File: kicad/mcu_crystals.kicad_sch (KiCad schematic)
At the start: 6 parts, among them X1 32MHz, X2 32kHz768

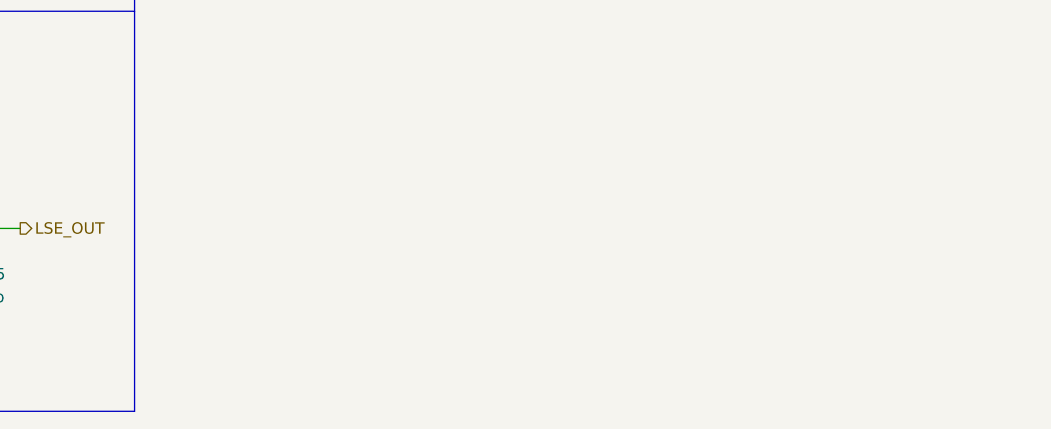
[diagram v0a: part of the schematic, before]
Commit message: feat(BOM): fill missing parts in BOM
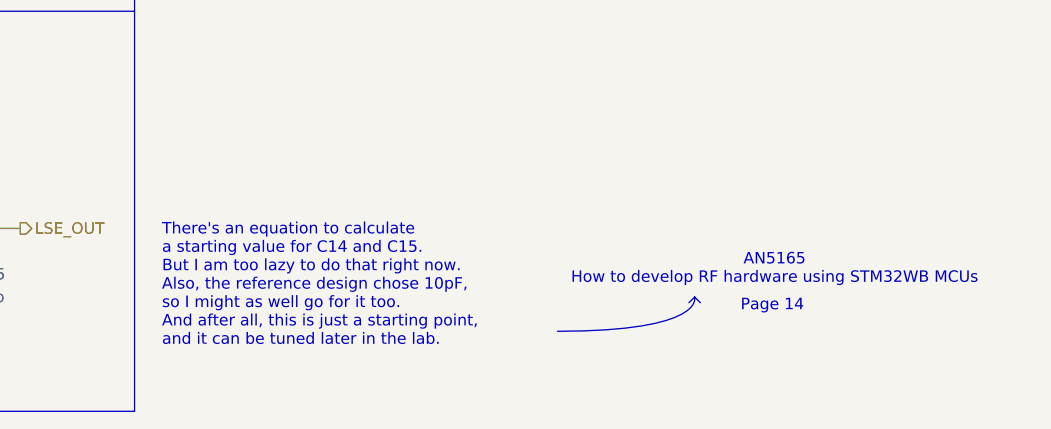
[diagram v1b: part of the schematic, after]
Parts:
- C14, C15: Distributor (none) -> LCSC; Distributor Link (none) -> https://www.lcsc.com/product-detail/C161520.html; MPN (none) -> GRM1555C1H100FA01D; Manufacturer (none) -> muRata
- R1, R2: Distributor (none) -> LCSC; Distributor Link (none) -> https://www.lcsc.com/product-detail/C190119.html; MPN (none) -> CRCW04020000Z0ED; Manufacturer (none) -> VISHAY
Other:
- note added: "AN5165 How to develop RF hardware using STM32WB MCUs"
- note added: "Page 14"
- note added: "There's an equation to calculate a starting value for C14 and C15. But I am too lazy to do that right now. Also, the reference design chose 10pF, so I might as well go for it too. And after all, this is just a starting point, and it can be tuned later in the lab."
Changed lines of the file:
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@@
 		(comment 4 "GitHub: https://github.com/odaij/stm32-bt-board")
+	)
+	(bezier
+		(pts
+			(xy 232.41 137.16) (xy 248.92 137.16) (xy 247.65 133.35) (xy 247.65 133.35)
+		)
+		(stroke
+			(width 0)
+			(type default)
+		)
+		(fill
+			(type none)
+		)
 	)
 	(rectangle
@@
 				(bold yes)
 			)
+		)
+	)
+	(text "Page 14"
+		(exclude_from_sim no)
+		(at 256.286 134.366 0)
+		(effects
+			(font
+				(size 1.27 1.27)
+			)
+		)
+	)
+	(text "AN5165\nHow to develop RF hardware using STM32WB MCUs\n"
+		(exclude_from_sim no)
+		(at 256.54 130.302 0)
+		(effects
+			(font
+				(size 1.27 1.27)
+			)
+			(href "https://www.st.com/resource/en/application_note/an5165-how-to-develop-rf-hardware-using-stm32wb-microcontrollers-stmicroelectronics.pdf")
+		)
+	)
+	(text "There's an equation to calculate\na starting value for C14 and C15.\nBut I am too lazy to do that right now.\nAlso, the reference design chose 10pF,\nso I might as well go for it too.\nAnd after all, this is just a starting point,\nand it can be tuned later in the lab."
+		(exclude_from_sim no)
+		(at 188.468 132.08 0)
+		(effects
+			(font
+				(size 1.27 1.27)
+			)
+			(justify left)
 		)
 	)
@@
 		(pts
 			(xy 163.83 135.89) (xy 163.83 138.43)
+		)
+		(stroke
+			(width 0)
+			(type default)
+		)
+	)
+	(polyline
+		(pts
+			(xy 247.65 133.35) (xy 248.285 133.985)
+		)
+		(stroke
+			(width 0)
+			(type default)
+		)
+	)
+	(polyline
+		(pts
+			(xy 247.015 133.985) (xy 247.65 133.35)
 		)
 		(stroke
@@
 			)
 		)
-		(property "Datasheet" ""
+		(property "Datasheet" "https://www.lcsc.com/datasheet/C190119.pdf"
 			(at 140.97 80.01 0)
 			(hide yes)
@@
 			)
 		)
-		(property "Description" "Resistor, small symbol"
+		(property "Description" "RES 0Ω 62.5mW 0402"
 			(at 140.97 80.01 0)
 			(hide yes)
@@
 			)
 		)
-		(property "Distributor" ""
+		(property "Distributor" "LCSC"
+			(at 140.97 80.01 90)
+			(hide yes)
+			(show_name no)
+			(do_not_autoplace no)
+			(effects
+				(font
+					(size 1.27 1.27)
+				)
+			)
+		)
+		(property "Distributor Link" "https://www.lcsc.com/product-detail/C190119.html"
+			(at 140.97 80.01 90)
+			(hide yes)
+			(show_name no)
+			(do_not_autoplace no)
+			(effects
+				(font
+					(size 1.27 1.27)
+				)
+			)
+		)
+		(property "MPN" "CRCW04020000Z0ED"
+			(at 140.97 80.01 90)
+			(hide yes)
+			(show_name no)
+			(do_not_autoplace no)
+			(effects
+				(font
+					(size 1.27 1.27)
+				)
+			)
+		)
+		(property "Manufacturer" "VISHAY"
 			(at 140.97 80.01 90)
 			(hide yes)
@@
 			)
 		)
-		(property "Datasheet" ""
+		(property "Datasheet" "https://www.lcsc.com/datasheet/C161520.pdf"
 			(at 163.83 132.08 0)
 			(hide yes)
@@
 			)
 		)
-		(property "Description" "Unpolarized capacitor"
+		(property "Description" "CAP CER 10pF 50V C0G 0402"
 			(at 163.83 132.08 0)
 			(hide yes)
@@
 			)
 		)
-		(property "Distributor Link" ""
+		(property "Distributor Link" "https://www.lcsc.com/product-detail/C161520.html"
 			(at 163.83 132.08 0)
 			(hide yes)
@@
 			)
 		)
-		(property "Manufacturer" ""
+		(property "Manufacturer" "muRata"
 			(at 163.83 132.08 0)
 			(hide yes)
@@
 			)
 		)
-		(property "Distributor" ""
+		(property "Distributor" "LCSC"
+			(at 163.83 132.08 0)
+			(hide yes)
+			(show_name no)
+			(do_not_autoplace no)
+			(effects
+				(font
+					(size 1.27 1.27)
+				)
+			)
+		)
+		(property "MPN" "GRM1555C1H100FA01D"
 			(at 163.83 132.08 0)
 			(hide yes)
@@
 			)
 		)
-		(property "Datasheet" ""
+		(property "Datasheet" "https://www.lcsc.com/datasheet/C161520.pdf"
 			(at 147.32 132.08 0)
 			(hide yes)
@@
 			)
 		)
-		(property "Description" "Unpolarized capacitor"
+		(property "Description" "CAP CER 10pF 50V C0G 0402"
 			(at 147.32 132.08 0)
 			(hide yes)
@@
 			)
 		)
-		(property "Distributor Link" ""
+		(property "Distributor Link" "https://www.lcsc.com/product-detail/C161520.html"
 			(at 147.32 132.08 0)
 			(hide yes)
@@
 			)
 		)
-		(property "Manufacturer" ""
+		(property "Manufacturer" "muRata"
 			(at 147.32 132.08 0)
 			(hide yes)
@@
 			)
 		)
-		(property "Distributor" ""
+		(property "Distributor" "LCSC"
+			(at 147.32 132.08 0)
+			(hide yes)
+			(show_name no)
+			(do_not_autoplace no)
+			(effects
+				(font
+					(size 1.27 1.27)
+				)
+			)
+		)
+		(property "MPN" "GRM1555C1H100FA01D"
 			(at 147.32 132.08 0)
 			(hide yes)
@@
 			)
 		)
-		(property "Datasheet" ""
+		(property "Datasheet" "https://www.lcsc.com/datasheet/C190119.pdf"
 			(at 140.97 125.73 0)
 			(hide yes)
@@
 			)
 		)
-		(property "Description" "Resistor, small symbol"
+		(property "Description" "RES 0Ω 62.5mW 0402"
 			(at 140.97 125.73 0)
 			(hide yes)
@@
 			)
 		)
-		(property "Distributor" ""
+		(property "Distributor" "LCSC"
 			(at 140.97 125.73 90)
 			(hide yes)
+			(show_name no)
+			(do_not_autoplace no)
+			(effects
+				(font
+					(size 1.27 1.27)
+				)
+			)
+		)
+		(property "Distributor Link" "https://www.lcsc.com/product-detail/C190119.html"
+			(at 140.97 125.73 90)
+			(hide yes)
+			(show_name no)
+			(do_not_autoplace no)
+			(effects
+				(font
+					(size 1.27 1.27)
+				)
+			)
+		)
+		(property "MPN" "CRCW04020000Z0ED"
+			(at 140.97 125.73 90)
+			(hide yes)
+			(show_name no)
+			(do_not_autoplace no)
+			(effects
+				(font
+					(size 1.27 1.27)
+				)
+			)
+		)
+		(property "Manufacturer" "VISHAY"
+			(at 140.97 125.73 90)
+			(hide yes)

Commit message: feat(manuf.): edit BOM and CPL to match JLCPCB's requirements
however, please pay close attention to the rotations during ordering, especially for the SOT components, as JLCPCB messes them up a bit, same for the connector and the filter
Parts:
- C14, C15: JLCPCB Part # (none) -> C161520
- R1, R2: JLCPCB Part # (none) -> C190119
- X1: Distributor Link https://www.lcsc.com/product-detail/crystals_ndk-nx2016sa-3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 -> https://www.lcsc.com/product-detail/C5441424.html; JLCPCB Part # (none) -> C5441424
- X2: Distributor Link https://www.lcsc.com/product-detail/C891748.html?s_z=s_p_NX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 -> https://www.lcsc.com/product-detail/C891748.html; JLCPCB Part # (none) -> C891748
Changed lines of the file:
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@@
-			)
-		)
-		(property "Distributor Link" "https://www.lcsc.com/product-detail/C190119.html"
-			(at 140.97 80.01 90)
-			(hide yes)
-			(show_name no)
-			(do_not_autoplace no)
-			(effects
-				(font
-					(size 1.27 1.27)
-				)
 			)
 		)
@@
 		)
 		(property "Manufacturer" "VISHAY"
+			(at 140.97 80.01 90)
+			(hide yes)
+			(show_name no)
+			(do_not_autoplace no)
+			(effects
+				(font
+					(size 1.27 1.27)
+				)
+			)
+		)
+		(property "JLCPCB Part #" "C190119"
+			(at 140.97 80.01 90)
+			(hide yes)
+			(show_name no)
+			(do_not_autoplace no)
+			(effects
+				(font
+					(size 1.27 1.27)
+				)
+			)
+		)
+		(property "Distributor Link" "https://www.lcsc.com/product-detail/C190119.html"
 			(at 140.97 80.01 90)
 			(hide yes)
@@
 			)
 		)
-		(property "Distributor Link" "https://www.lcsc.com/product-detail/C891748.html?s_z=s_p_NX2012SA-32.768KHZ-STD-MUB-2&spm=wm.fly.bg.0.xh&lcsc_vid=RlRYUFFURFcNVFIDFVMMXgZSRlJeUABSQVNfAwJfQwIxVlNeTldcXlVQRFddVjsOAxUeFF5JWBYZEEoKFBINSQcJGk4eFQsCAgIaSgADAwAHC0slRFBXUFJeQ08GEwkK"
-			(at 156.21 125.73 0)
-			(hide yes)
-			(show_name no)
-			(do_not_autoplace no)
-			(effects
-				(font
-					(size 1.27 1.27)
-				)
-			)
-		)
 		(property "Manufacturer" "NDK"
 			(at 156.21 125.73 0)
@@
 		)
 		(property "MPN" "NX2012SA-32.768KHZ-STD-MUB-2"
+			(at 156.21 125.73 0)
+			(hide yes)
+			(show_name no)
+			(do_not_autoplace no)
+			(effects
+				(font
+					(size 1.27 1.27)
+				)
+			)
+		)
+		(property "JLCPCB Part #" "C891748"
+			(at 156.21 125.73 0)
+			(hide yes)
+			(show_name no)
+			(do_not_autoplace no)
+			(effects
+				(font
+					(size 1.27 1.27)
+				)
+			)
+		)
+		(property "Distributor Link" "https://www.lcsc.com/product-detail/C891748.html"
 			(at 156.21 125.73 0)
 			(hide yes)
@@
 			)
 		)
-		(property "Distributor Link" "https://www.lcsc.com/product-detail/crystals_ndk-nx2016sa-32mhz-exs00a-cs06654_C5441424.html"
-			(at 156.21 80.01 0)
-			(hide yes)
-			(show_name no)
-			(do_not_autoplace no)
-			(effects
-				(font
-					(size 1.27 1.27)
-				)
-			)
-		)
 		(property "Manufacturer" "NDK"
 			(at 156.21 80.01 0)
@@
 		)
 		(property "MPN" "NX2016SA-32MHZ-EXS00A-CS06654"
+			(at 156.21 80.01 0)
+			(hide yes)
+			(show_name no)
+			(do_not_autoplace no)
+			(effects
+				(font
+					(size 1.27 1.27)
+				)
+			)
+		)
+		(property "JLCPCB Part #" "C5441424"
+			(at 156.21 80.01 0)
+			(hide yes)
+			(show_name no)
+			(do_not_autoplace no)
+			(effects
+				(font
+					(size 1.27 1.27)
+				)
+			)
+		)
+		(property "Distributor Link" "https://www.lcsc.com/product-detail/C5441424.html"
 			(at 156.21 80.01 0)
 			(hide yes)
@@
 			)
 		)
-		(property "Distributor Link" "https://www.lcsc.com/product-detail/C161520.html"
-			(at 163.83 132.08 0)
-			(hide yes)
-			(show_name no)
-			(do_not_autoplace no)
-			(effects
-				(font
-					(size 1.27 1.27)
-				)
-			)
-		)
 		(property "Manufacturer" "muRata"
 			(at 163.83 132.08 0)
@@
 		)
 		(property "MPN" "GRM1555C1H100FA01D"
+			(at 163.83 132.08 0)
+			(hide yes)
+			(show_name no)
+			(do_not_autoplace no)
+			(effects
+				(font
+					(size 1.27 1.27)
+				)
+			)
+		)
+		(property "JLCPCB Part #" "C161520"
+			(at 163.83 132.08 0)
+			(hide yes)
+			(show_name no)
+			(do_not_autoplace no)
+			(effects
+				(font
+					(size 1.27 1.27)
+				)
+			)
+		)
+		(property "Distributor Link" "https://www.lcsc.com/product-detail/C161520.html"
 			(at 163.83 132.08 0)
 			(hide yes)
@@
 			)
 		)
-		(property "Distributor Link" "https://www.lcsc.com/product-detail/C161520.html"
-			(at 147.32 132.08 0)
-			(hide yes)
-			(show_name no)
-			(do_not_autoplace no)
-			(effects
-				(font
-					(size 1.27 1.27)
-				)
-			)
-		)
 		(property "Manufacturer" "muRata"
 			(at 147.32 132.08 0)
@@
 		)
 		(property "MPN" "GRM1555C1H100FA01D"
+			(at 147.32 132.08 0)
+			(hide yes)
+			(show_name no)
+			(do_not_autoplace no)
+			(effects
+				(font
+					(size 1.27 1.27)
+				)
+			)
+		)
+		(property "JLCPCB Part #" "C161520"
+			(at 147.32 132.08 0)
+			(hide yes)
+			(show_name no)
+			(do_not_autoplace no)
+			(effects
+				(font
+					(size 1.27 1.27)
+				)
+			)
+		)
+		(property "Distributor Link" "https://www.lcsc.com/product-detail/C161520.html"
 			(at 147.32 132.08 0)
 			(hide yes)
@@
 			)
 		)
+		(property "MPN" "CRCW04020000Z0ED"
+			(at 140.97 125.73 90)
+			(hide yes)
+			(show_name no)
+			(do_not_autoplace no)
+			(effects
+				(font
+					(size 1.27 1.27)
+				)
+			)
+		)
+		(property "Manufacturer" "VISHAY"
+			(at 140.97 125.73 90)
+			(hide yes)
+			(show_name no)
+			(do_not_autoplace no)
+			(effects
+				(font
+					(size 1.27 1.27)
+				)
+			)
+		)
+		(property "JLCPCB Part #" "C190119"
+			(at 140.97 125.73 90)
+			(hide yes)
+			(show_name no)
+			(do_not_autoplace no)
+			(effects
+				(font
+					(size 1.27 1.27)
+				)
+			)
+		)
 		(property "Distributor Link" "https://www.lcsc.com/product-detail/C190119.html"
 			(at 140.97 125.73 90)
 			(hide yes)
-			(show_name no)
-			(do_not_autoplace no)
-			(effects
-				(font
-					(size 1.27 1.27)
-				)
-			)
-		)
-		(property "MPN" "CRCW04020000Z0ED"
-			(at 140.97 125.73 90)
-			(hide yes)
-			(show_name no)
-			(do_not_autoplace no)
-			(effects
-				(font
-					(size 1.27 1.27)
-				)
-			)
-		)
-		(property "Manufacturer" "VISHAY"
-			(at 140.97 125.73 90)
-			(hide yes)
